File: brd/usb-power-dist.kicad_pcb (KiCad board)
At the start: 2 copper layers, 50 x 50 mm, 40 parts, among them J1 POWER IN, J2 USB_A, J3 USB_A, J4 CASC IN, J5 CASC OUT, U1 TPS2552D, U2 TPS2552D, U3 TPS2513

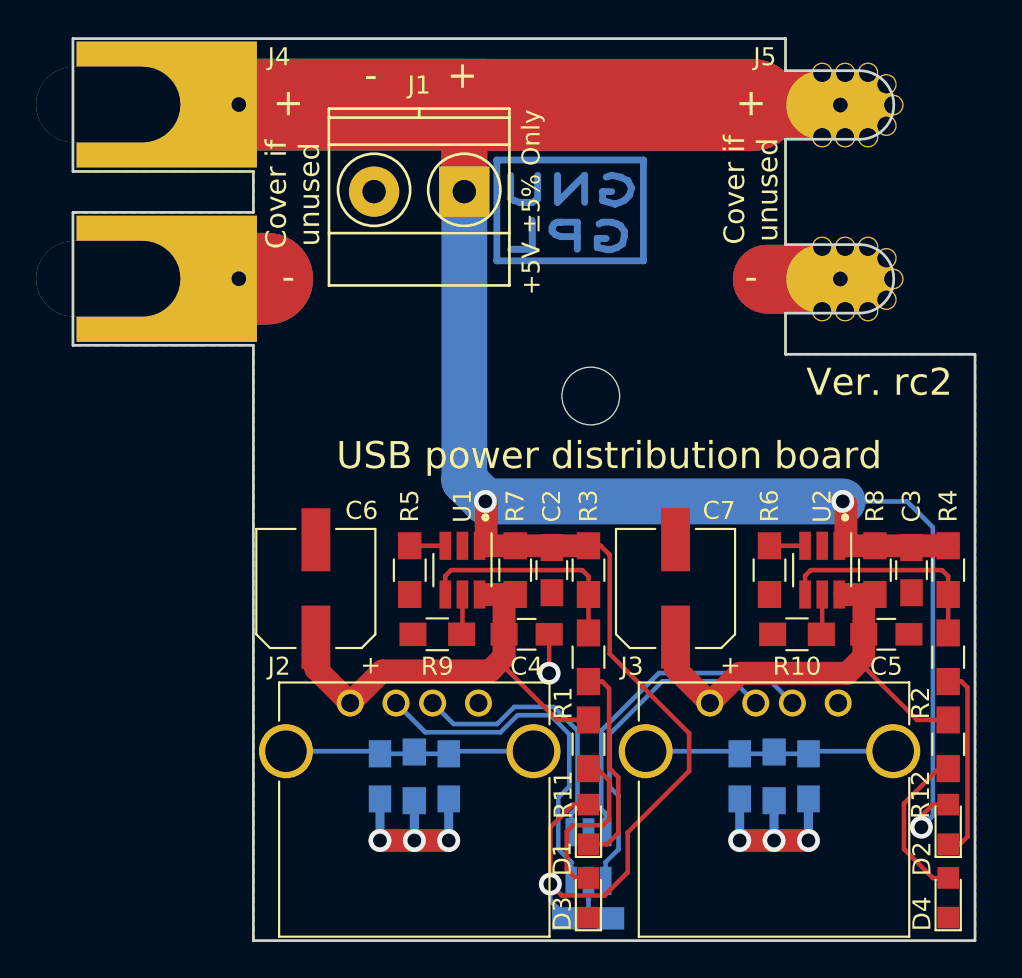
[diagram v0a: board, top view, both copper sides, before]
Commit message: descartado plateado de contactos mediante vias, reducidas tolerancias en su lugar
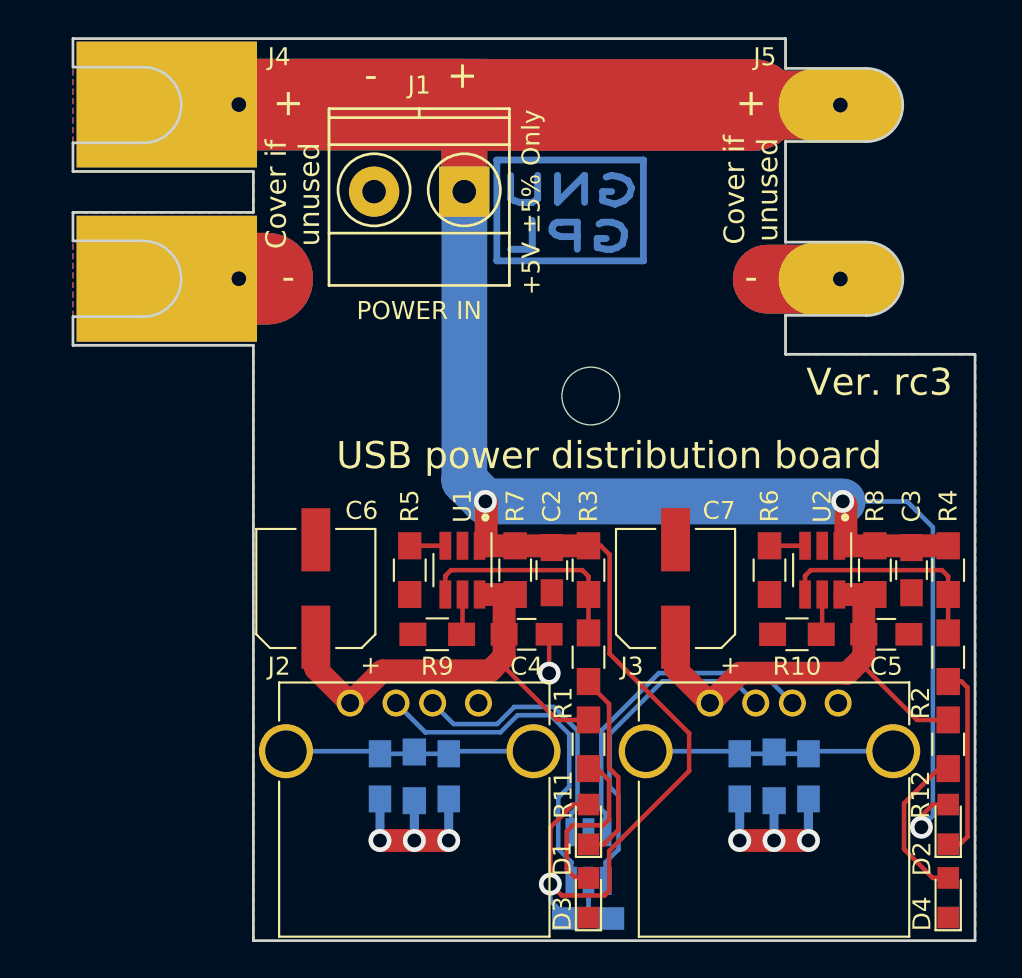
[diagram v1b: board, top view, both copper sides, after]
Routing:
- net Net-(D1-Pad1): track 11.4 -> 10.9 mm
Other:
- outline, holes or cut-outs redrawn
- board text added: "SN:k099C8134d_3617"
- board text added: "Ver. rc3"
- board text removed: "Ver. rc2"
- board text removed: "k099C8134/3-d0917"

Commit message: recolocados componentes a una única cara y retrazadas pistas, a falta de serigrafía !wip
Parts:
- removed the R3 at (151.5, 110.5)
- removed the R4 at (171.4, 110.5)
- removed the R5 at (141.6, 110.5)
- removed the R6 at (161.5, 110.5)
- removed the R7 at (147.4, 110.5)
- removed the R8 at (167.4, 110.5)
- added F1: 3A, Fuse_Holders_and_Fuses:Fuse_SMD1206_Wave, F.Cu at (147.3, 113.8)
- added F2: 3A, Fuse_Holders_and_Fuses:Fuse_SMD1206_Wave, F.Cu at (167.1, 113.8)
- added L1: Choke, Inductors_SMD:L_0805_HandSoldering, F.Cu at (140.7, 113.8)
- added L2: Choke, Inductors_SMD:L_0805_HandSoldering, F.Cu at (160.5, 113.8)
- C10, C11, C8, C9, U3: moved to F.Cu
- C3: renamed from C1; moved to F.Cu
- C6, C7: value 100uF -> 220uF; footprint Capacitors_SMD:CP_Elec_6.3x5.3 -> Capacitors_SMD:CP_Elec_6.3x7.7
- R1, R2: value 470R -> 330R
- R7: renamed from R13; moved to F.Cu
- R8: renamed from R14; moved to F.Cu
- moved C3 23.1 mm to (151.4, 106.7)
- moved U3 16.1 mm to (151.4, 110.2), turned to 90 degrees
- moved C8 12.2 mm to (134.6, 113.8), turned to 90 degrees
- moved C11 9.79 mm to (154.4, 113.8), turned to 90 degrees
- moved R8 9.72 mm to (156.5, 113.8), turned to 90 degrees
- moved R7 9.65 mm to (136.7, 113.8), turned to 90 degrees
- moved C9 9.65 mm to (158.5, 113.8), turned to 90 degrees
- moved C10 8.23 mm to (138.7, 113.8), turned to 90 degrees
- moved R3 7.90 mm to (143.8, 106.2), turned to 0 degrees
- moved R4 7.89 mm to (163.6, 106.2), turned to 0 degrees
- moved C6 5.48 mm to (137.7, 106.2)
- moved C5 5.47 mm to (162.6, 113.8), turned to 270 degrees
- moved C7 5.46 mm to (157.5, 106.2)
- moved C4 5.34 mm to (142.7, 113.8), turned to 270 degrees
- moved C2 2.90 mm to (167.1, 108.7), turned to 90 degrees
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- renumbered C2 to C1, C3 to C2, J4 to J2, J5 to J3, J2 to J4, J3 to J5, R9 to R3, R10 to R4, R11 to R5, R12 to R6
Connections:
- net Net-(J2-Pad2) renamed /D1-
- net Net-(J2-Pad3) renamed /D1+
- net Net-(J3-Pad2) renamed /D2-
- net Net-(J3-Pad3) renamed /D2+
- J4 pad 1: Net-(C4-Pad1) -> Net-(J4-Pad1)
- J5 pad 1: Net-(C5-Pad1) -> Net-(J5-Pad1)
- U1 pad 3: Net-(R5-Pad1) -> GND
- U2 pad 3: Net-(R6-Pad1) -> GND
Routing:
- net GND: track 36.0 -> 12.3 mm, vias 7 -> 0
- net +5V: track 193.4 -> 179.2 mm, vias 4 -> 5
- net Net-(C11-Pad1): track 13.9 -> 23.5 mm
- net Net-(C10-Pad1): track 13.9 -> 23.4 mm
- net /D1-: track 19.8 -> 13.6 mm, vias 0 -> 1
- net Net-(J4-Pad1): track 0.00 -> 3.82 mm
- net Net-(J5-Pad1): track 0.00 -> 3.77 mm
- net /D2-: track 18.4 -> 15.5 mm, vias 0 -> 1
- net /D2+: track 18.3 -> 15.5 mm, vias 0 -> 1
- net Net-(C4-Pad1): track 25.4 -> 22.8 mm
- net Net-(C5-Pad1): track 25.4 -> 22.9 mm
- net Net-(R4-Pad1): track 2.23 -> 4.42 mm
- net Net-(R3-Pad1): track 2.23 -> 4.41 mm
- net Net-(R5-Pad1): track 1.97 -> 0.00 mm
- net Net-(R6-Pad1): track 1.97 -> 0.00 mm
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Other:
- rule trace_min: 0.2 -> 0.2032
- rule via_min_drill: 0.3 -> 0.4064
- rule via_min_size: 0.4 -> 0.6096
- board text added: "Current R3/R4 100mA 226k 500mA 52k3 900mA 28k7 1500mA 16k9 No lim See doc"
- board text added: "Ver. 1.0"
- board text removed: "Current R9/R10 100mA 226k 500mA 52k3 900mA 28k7 1500mA 16k9 No lim See doc"
- board text removed: "Ver. rc3"

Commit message: editada serigrafía a falta de SN
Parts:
- moved C3 0.25 mm to (151.1, 106.7)
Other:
- board text added: "Current R3/R4 100mA 226k 500mA 52k3 900mA 28k7 1500mA 16k9 ** No lim See doc"
- board text removed: "Current R3/R4 100mA 226k 500mA 52k3 900mA 28k7 1500mA 16k9 No lim See doc"
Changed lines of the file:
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@@
     (area 122.860999 80.950999 173.011001 131.101001)
     (thickness 1.6)
-    (drawings 78)
-    (tracks 282)
+    (drawings 86)
+    (tracks 281)
     (zones 0)
     (modules 38)
@@
     (tags "Fuse Sicherung SMD1206 Littlefuse-Wickmann 433 Series Wave ")
     (attr smd)
-    (fp_text reference F1 (at -0.05 -2.2 270) (layer F.SilkS)
+    (fp_text reference F1 (at -0.05 2.032 270) (layer F.SilkS)
       (effects (font (size 1 1) (thickness 0.15)))
     )
@@
     (tags "SOT-23-6 Handsoldering")
     (attr smd)
-    (fp_text reference U3 (at -1.397 -2.667 270) (layer F.SilkS)
+    (fp_text reference U3 (at -3.302 -1.778 270) (layer F.SilkS)
       (effects (font (size 1 1) (thickness 0.15)))
     )
@@
     (tags "SOT-23-6 Handsoldering")
     (attr smd)
-    (fp_text reference U1 (at -3.556 0 180) (layer F.SilkS)
+    (fp_text reference U1 (at -1.016 -2.54 180) (layer F.SilkS)
       (effects (font (size 1 1) (thickness 0.15)))
     )
@@
     (tags "capacitor 0805")
     (attr smd)
-    (fp_text reference C1 (at -3.556 0 90) (layer F.SilkS)
+    (fp_text reference C1 (at 0 1.778 90) (layer F.SilkS)
       (effects (font (size 1 1) (thickness 0.15)))
     )
@@
   )
   (module Capacitors_SMD:C_0805_HandSoldering (layer F.Cu)
-    (at 151.384 106.68)
+    (at 151.13 106.68)
     (descr "Capacitor SMD 0805, hand soldering")
     (tags "capacitor 0805")
     (attr smd)
-    (fp_text reference C3 (at -3.155 0.254 270) (layer F.SilkS)
+    (fp_text reference C3 (at 0 -1.524) (layer F.SilkS)
       (effects (font (size 1 1) (thickness 0.15)))
     )
@@
     (tags "capacitor 0805")
     (attr smd)
-    (fp_text reference C2 (at -3.556 0 90) (layer F.SilkS)
+    (fp_text reference C2 (at 0 1.778 90) (layer F.SilkS)
       (effects (font (size 1 1) (thickness 0.15)))
     )
@@
     (tags "capacitor 0805")
     (attr smd)
-    (fp_text reference C4 (at 0 1.778 270) (layer F.SilkS)
+    (fp_text reference C4 (at -14.224 2.032 270) (layer F.SilkS)
       (effects (font (size 1 1) (thickness 0.15)))
     )
@@
     (tags "capacitor 0805")
     (attr smd)
-    (fp_text reference C5 (at 0 1.778 270) (layer F.SilkS)
+    (fp_text reference C5 (at -14.224 2.032 270) (layer F.SilkS)
       (effects (font (size 1 1) (thickness 0.15)))
     )
@@
     (tags "capacitor 0805")
     (attr smd)
-    (fp_text reference C8 (at 5.334 0 90) (layer F.SilkS)
+    (fp_text reference C8 (at 14.224 0 90) (layer F.SilkS)
       (effects (font (size 1 1) (thickness 0.15)))
     )
@@
     (tags "capacitor 0805")
     (attr smd)
-    (fp_text reference C9 (at 5.334 0.127 90) (layer F.SilkS)
+    (fp_text reference C9 (at 14.224 -1.016 90) (layer F.SilkS)
       (effects (font (size 1 1) (thickness 0.15)))
     )
@@
     (tags "capacitor 0805")
     (attr smd)
-    (fp_text reference C10 (at 5.842 0 90) (layer F.SilkS)
+    (fp_text reference C10 (at 14.224 -1.016 90) (layer F.SilkS)
       (effects (font (size 1 1) (thickness 0.15)))
     )
@@
     (tags "capacitor 0805")
     (attr smd)
-    (fp_text reference C11 (at 5.842 0.127 90) (layer F.SilkS)
+    (fp_text reference C11 (at 14.224 0 90) (layer F.SilkS)
       (effects (font (size 1 1) (thickness 0.15)))
     )
@@
     (descr "USB A connector")
     (tags "USB USB_A")
-    (fp_text reference J4 (at -3.937 -2.032) (layer F.SilkS)
+    (fp_text reference J4 (at 6.477 -2.032) (layer F.SilkS)
       (effects (font (size 1 1) (thickness 0.15)))
     )
@@
     (descr "USB A connector")
     (tags "USB USB_A")
-    (fp_text reference J5 (at -4.318 -2.032) (layer F.SilkS)
+    (fp_text reference J5 (at 6.35 -2.032) (layer F.SilkS)
       (effects (font (size 1 1) (thickness 0.15)))
     )
@@
     (tags "resistor 0805")
     (attr smd)
-    (fp_text reference R7 (at 5.842 0.127 90) (layer F.SilkS)
+    (fp_text reference R7 (at 14.224 -0.508 90) (layer F.SilkS)
       (effects (font (size 1 1) (thickness 0.15)))
     )
@@
     (tags "resistor 0805")
     (attr smd)
-    (fp_text reference R8 (at 5.842 0 90) (layer F.SilkS)
+    (fp_text reference R8 (at 14.224 -0.508 90) (layer F.SilkS)
       (effects (font (size 1 1) (thickness 0.15)))
     )
@@
     (tags "SOT-23-6 Handsoldering")
     (attr smd)
-    (fp_text reference U2 (at -3.556 0 180) (layer F.SilkS)
+    (fp_text reference U2 (at -1.016 -2.54 180) (layer F.SilkS)
       (effects (font (size 1 1) (thickness 0.15)))
     )
@@
     (descr "SMT capacitor, aluminium electrolytic, 6.3x7.7")
     (attr smd)
-    (fp_text reference C6 (at 0 4.43 90) (layer F.SilkS)
+    (fp_text reference C6 (at 4.064 2.54 180) (layer F.SilkS)
       (effects (font (size 1 1) (thickness 0.15)))
     )
@@
     (descr "SMT capacitor, aluminium electrolytic, 6.3x7.7")
     (attr smd)
-    (fp_text reference C7 (at 0 4.43 90) (layer F.SilkS)
+    (fp_text reference C7 (at 4.064 2.54 180) (layer F.SilkS)
       (effects (font (size 1 1) (thickness 0.15)))
     )
@@
     (tags "Fuse Sicherung SMD1206 Littlefuse-Wickmann 433 Series Wave ")
     (attr smd)
-    (fp_text reference F2 (at -0.05 -2.2 270) (layer F.SilkS)
+    (fp_text reference F2 (at -0.05 2.032 270) (layer F.SilkS)
       (effects (font (size 1 1) (thickness 0.15)))
     )
@@
     (tags "resistor 0805")
     (attr smd)
-    (fp_text reference L1 (at 0 -2.1 270) (layer F.SilkS)
+    (fp_text reference L1 (at -14.224 1.524 270) (layer F.SilkS)
       (effects (font (size 1 1) (thickness 0.15)))
     )
@@
     (tags "resistor 0805")
     (attr smd)
-    (fp_text reference L2 (at 0 -2.1 270) (layer F.SilkS)
+    (fp_text reference L2 (at -14.224 1.524 270) (layer F.SilkS)
       (effects (font (size 1 1) (thickness 0.15)))
     )
@@
     )
   )
+  (gr_text "USB power\ndistribution\nboard" (at 153.924 89.662 90) (layer F.SilkS)
+    (effects (font (size 1.5 1.5) (thickness 0.3)))
+  )
+  (gr_line (start 153.416 101.854) (end 153.924 100.838) (layer F.SilkS) (width 0.15))
+  (gr_line (start 153.416 116.332) (end 153.416 101.854) (layer F.SilkS) (width 0.15))
+  (gr_line (start 163.576 111.252) (end 153.416 111.252) (layer F.SilkS) (width 0.15))
+  (gr_line (start 163.576 116.332) (end 163.576 111.252) (layer F.SilkS) (width 0.15))
+  (gr_line (start 143.764 111.252) (end 133.604 111.252) (layer F.SilkS) (width 0.15))
+  (gr_line (start 143.764 116.332) (end 143.764 111.252) (layer F.SilkS) (width 0.15))
+  (gr_line (start 133.604 101.6) (end 133.604 116.332) (layer F.SilkS) (width 0.15))
+  (gr_line (start 134.112 100.838) (end 133.604 101.6) (layer F.SilkS) (width 0.15))
   (dimension 6.5 (width 0.3) (layer Dwgs.User)
     (gr_text "6,500 mm" (at 165.65 76.9) (layer Dwgs.User)
@@
   (gr_line (start 172.212 100.584) (end 159.258 100.584) (layer B.SilkS) (width 0.2))
   (gr_circle (center 149.352 112.395) (end 149.479 112.395) (layer F.SilkS) (width 0.2))
-  (gr_text "Current  R3/R4\n100mA   226k\n500mA   52k3\n900mA   28k7\n1500mA  16k9\nNo lim   See doc" (at 172.212 104.14) (layer B.SilkS)
+  (gr_text "Current  R3/R4\n100mA   226k\n500mA   52k3\n900mA   28k7\n1500mA  16k9 **\nNo lim   See doc" (at 172.212 104.14) (layer B.SilkS)
     (effects (font (size 1 1) (thickness 0.25)) (justify left mirror))
   )
-  (gr_circle (center 165.608 110.744) (end 165.735 110.744) (layer F.SilkS) (width 0.2))
-  (gr_circle (center 145.796 110.744) (end 145.923 110.744) (layer F.SilkS) (width 0.2))
+  (gr_circle (center 165.862 110.744) (end 165.989 110.744) (layer F.SilkS) (width 0.2))
+  (gr_circle (center 146.05 110.744) (end 146.177 110.744) (layer F.SilkS) (width 0.2))
   (gr_text "Sch\nPcb\nMechanical 3D\nDoc\nBoM\nCommercial use" (at 196.85 104.902) (layer Cmts.User)
     (effects (font (size 1.5 1.5) (thickness 0.3)))
@@
   (gr_text "Released under GNU/GPL 3 License\nhttps://www.gnu.org/licenses/gpl.html" (at 148.209 84.709) (layer B.SilkS)
     (effects (font (size 0.762 0.762) (thickness 0.15)) (justify mirror))
-  )
-  (gr_text "USB power distribution board" (at 152.654 104.14) (layer F.SilkS)
-    (effects (font (size 1.5 1.5) (thickness 0.3)))
   )
   (gr_text - (at 139.446 83.058) (layer F.SilkS)
@@
     (arrow2b (pts (xy 114.681 81.026) (xy 115.267421 82.152504)))
   )
+  (segment (start 148.783201 106.68) (end 150.177321 106.68) (width 0.635) (layer F.Cu) (net 1))
+  (segment (start 150.177321 106.68) (end 151.384 107.886679) (width 0.635) (layer F.Cu) (net 1))
+  (segment (start 151.384 107.886679) (end 151.384 108.886) (width 0.635) (layer F.Cu) (net 1))
   (segment (start 148.844 104.14) (end 168.656 104.14) (width 2.54) (layer B.Cu) (net 1))
   (segment (start 168.656 104.14) (end 168.669006 104.153006) (width 2.54) (layer B.Cu) (net 1))
@@
   (segment (start 148.783201 108.882561) (end 147.703762 109.962) (width 1.27) (layer F.Cu) (net 1))
   (segment (start 148.783201 106.68) (end 148.783201 108.882561) (width 1.27) (layer F.Cu) (net 1))
-  (segment (start 150.134 106.68) (end 150.546582 106.68) (width 0.635) (layer F.Cu) (net 1))
-  (segment (start 150.546582 106.68) (end 151.384 107.517418) (width 0.635) (layer F.Cu) (net 1))
-  (segment (start 151.384 107.517418) (end 151.384 108.886) (width 0.635) (layer F.Cu) (net 1))
   (segment (start 169.672 124.46) (end 169.672209 124.46) (width 0.254) (layer F.Cu) (net 1))
   (segment (start 169.672209 124.46) (end 170.643265 123.488944) (width 0.254) (layer F.Cu) (net 1))
@@
   (segment (start 167.132 112.212) (end 167.132 109.962) (width 1.27) (layer F.Cu) (net 1))
   (segment (start 147.32 112.212) (end 147.32 109.962) (width 1.27) (layer F.Cu) (net 1))
-  (segment (start 150.134 106.68) (end 148.783201 106.68) (width 0.635) (layer F.Cu) (net 1))
   (segment (start 145.114 109.662) (end 147.02 109.662) (width 0.635) (layer F.Cu) (net 1))
   (segment (start 147.02 109.662) (end 147.32 109.962) (width 0.635) (layer F.Cu) (net 1))

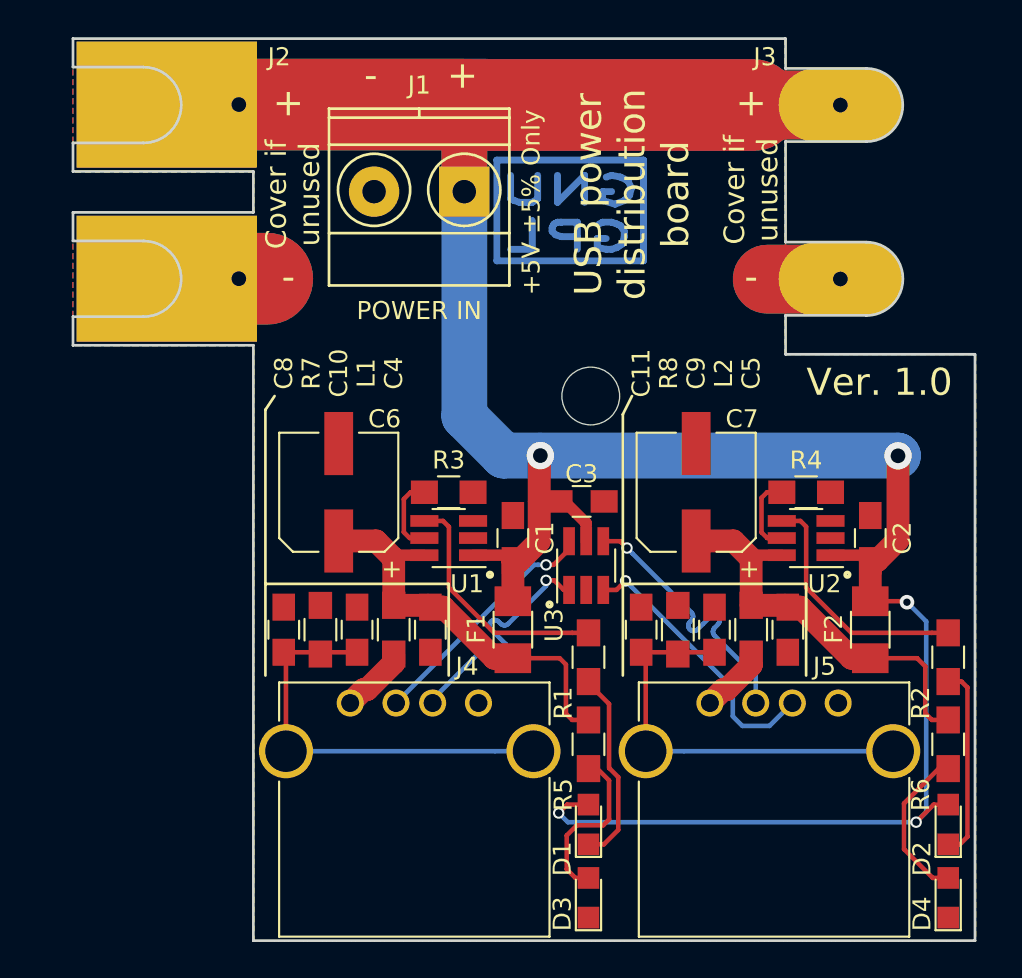
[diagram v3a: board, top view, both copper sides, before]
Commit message: corregida colocacion de componentes invertidos y próximos, retocados trazados y tamaños de pad, editadas capas invisibles, establecido nuevo SN
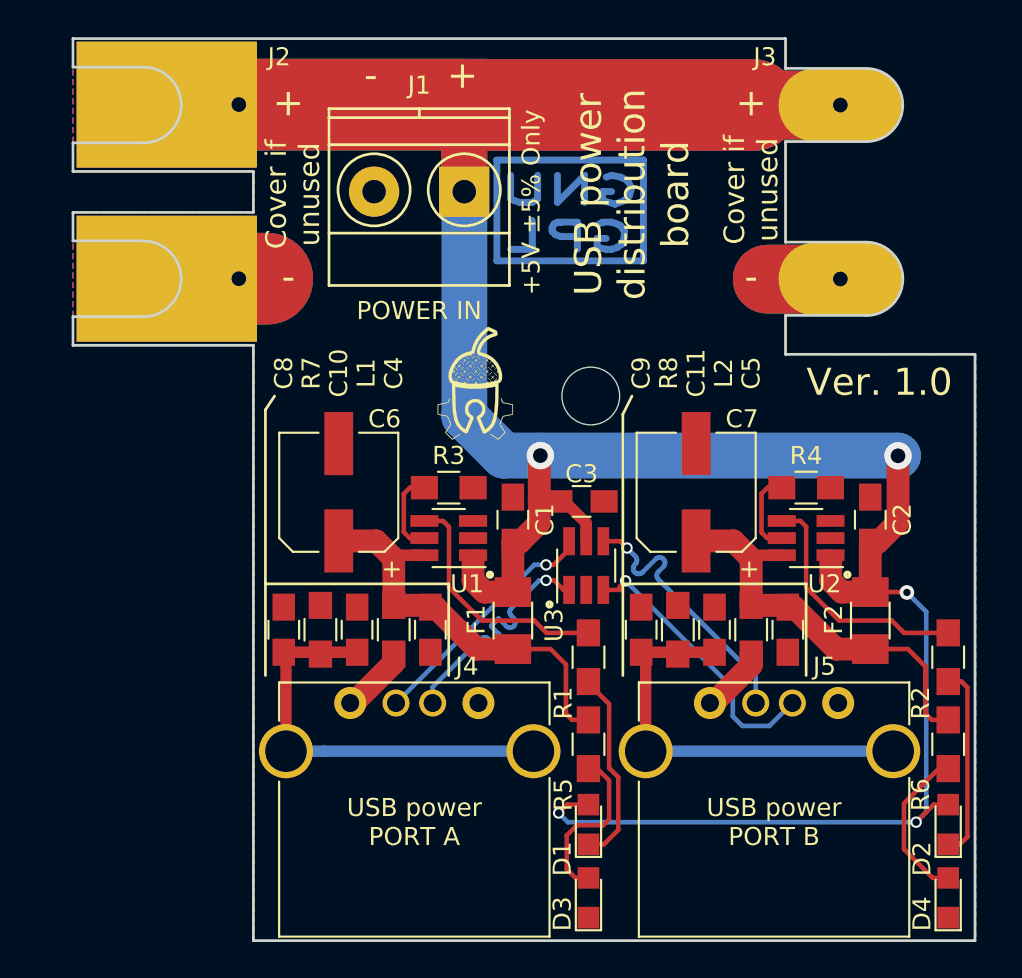
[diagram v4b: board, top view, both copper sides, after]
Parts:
- added G***: LOGO, brd:akorn-logo-small, F.Cu at (145.5, 100.1)
- moved C11 4.06 mm to (158.5, 113.8)
- moved C9 4.06 mm to (154.4, 113.8)
- moved C1 1.02 mm to (147.3, 107.7)
- moved C2 1.02 mm to (167.1, 107.7)
- moved F1 0.51 mm to (147.3, 113.3)
- moved F2 0.51 mm to (167.1, 113.3)
- moved R3 0.25 mm to (143.8, 105.9)
- moved R4 0.25 mm to (163.6, 105.9)
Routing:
- net +5V: track 178.9 -> 181.0 mm
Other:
- board text added: "SN:k698F61A900e_4417"
- board text added: "USB power PORT A"
- board text added: "USB power PORT B"
- board text removed: "SN:k099C8134d_3617"
